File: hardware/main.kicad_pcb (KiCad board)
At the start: 2 copper layers, 80 x 68.3 mm, 17 parts, among them J3 Conn_01x01_Pin, J4 Conn_01x01_Pin, J5 Conn_01x01_Pin, J6 Conn_01x01_Pin, K2 ADW11

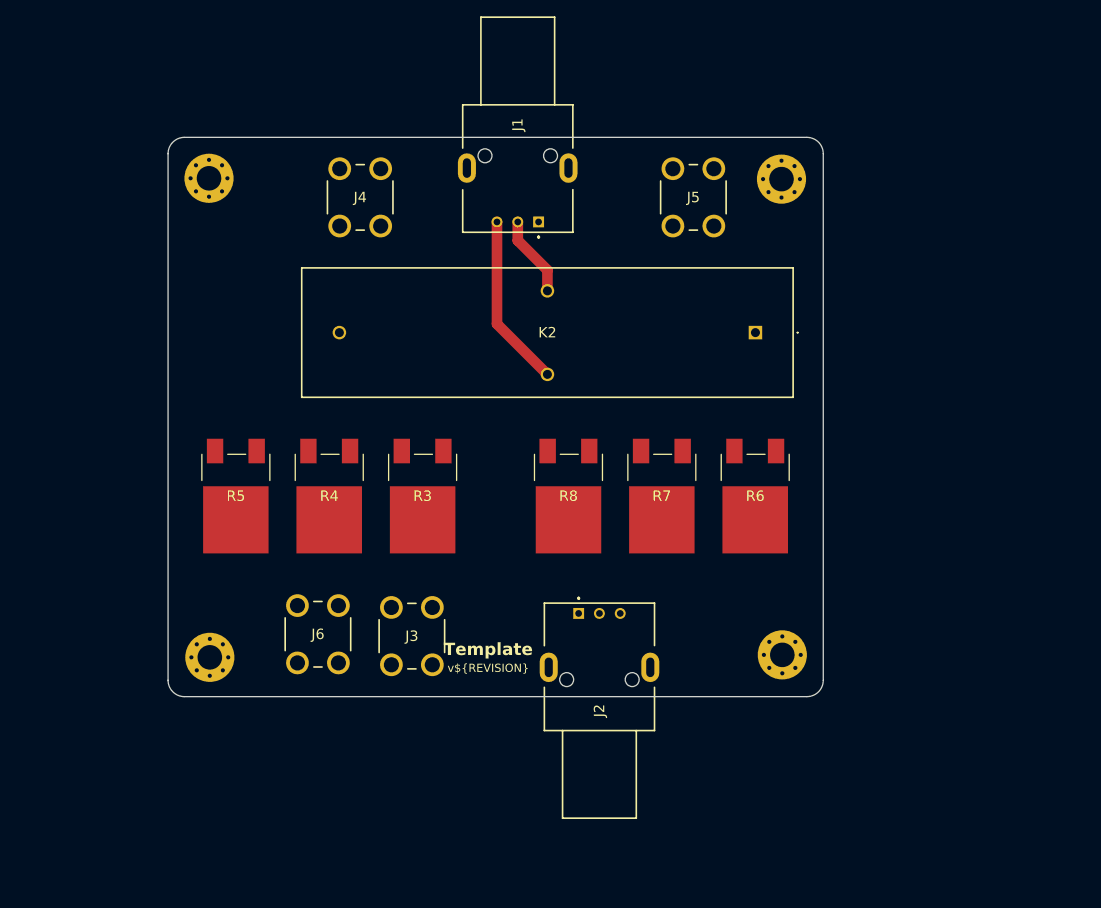
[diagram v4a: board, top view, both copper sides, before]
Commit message: changed resistors
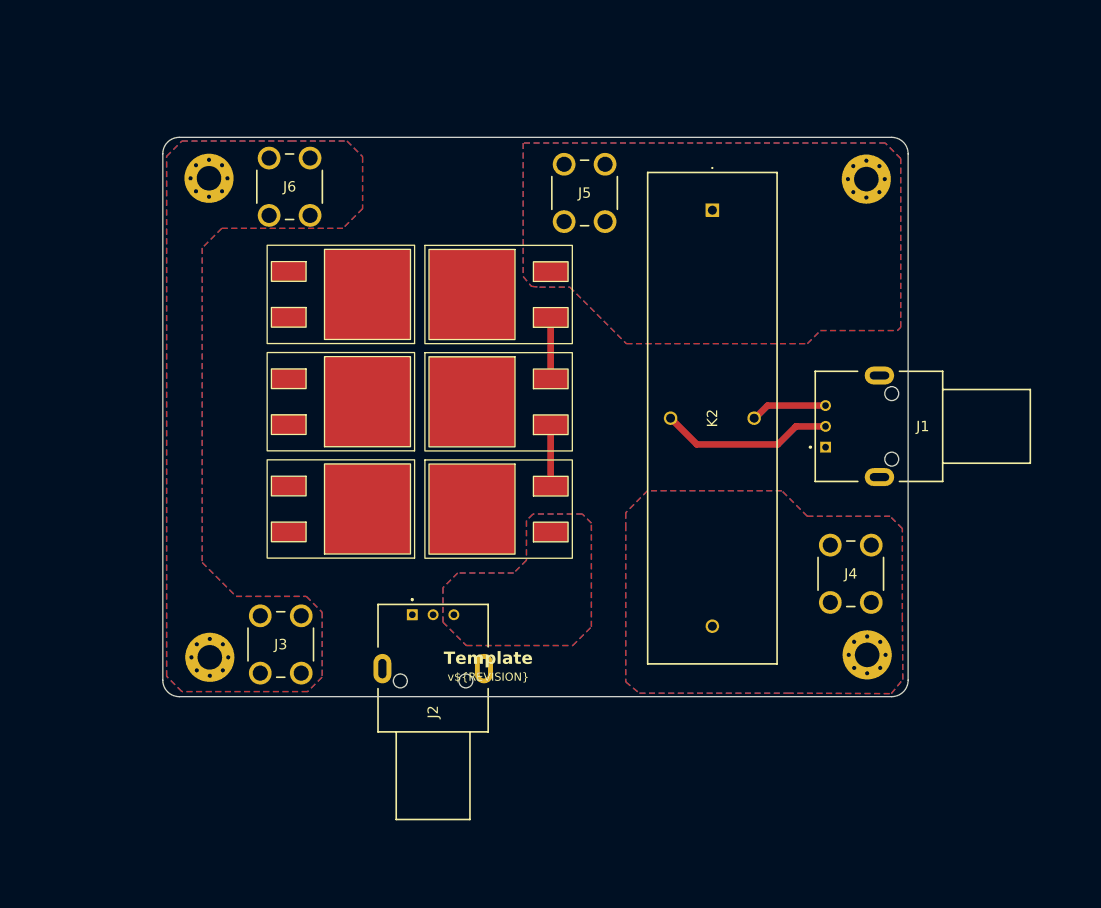
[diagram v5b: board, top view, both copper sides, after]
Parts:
- removed R3, R4, R5, R6, R7, R8: TKH45P5K00FE-TR, TKH45P5K00FE-TR:TKH45P50R0FETR
- added PWR263S-35-5001F1: ~, 7696:PWR263S-35-5001F, F.Cu at (135.7, 66.9)
- added PWR263S-35-5001F2: ~, 7696:PWR263S-35-5001F, F.Cu at (135.7, 80.0)
- added PWR263S-35-5001F3: ~, 7696:PWR263S-35-5001F, F.Cu at (135.7, 93.1)
- added PWR263S-35-5001F4: ~, 7696:PWR263S-35-5001F, F.Cu at (159.0, 93.1)
- added PWR263S-35-5001F5: ~, 7696:PWR263S-35-5001F, F.Cu at (159.0, 80.0)
- added PWR263S-35-5001F6: ~, 7696:PWR263S-35-5001F, F.Cu at (159.0, 66.9)
- moved J4 75.5 mm to (197.5, 104.5)
- moved J6 54.7 mm to (134.0, 50.2)
- moved J1 44.5 mm to (196.9, 85.5), turned to 0 degrees
- moved J2 20.3 mm to (146.5, 106.0)
- moved J3 16.0 mm to (132.9, 106.1)
- moved K2 15.8 mm to (183.1, 56.6), turned to -90 degrees
- moved J5 13.3 mm to (165.0, 58.0)
- moved REF** 10.4 mm to (201.9, 52.8)
- moved REF** 10.4 mm to (202.0, 110.9)
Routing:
- net GND: track 21.2 -> 9.50 mm
- net SD+: track 9.91 -> 21.2 mm
- net Net-(PWR263S-35-5001F5-Pad2): track 0.00 -> 7.50 mm
- net Net-(PWR263S-35-5001F4-Pad2): track 0.00 -> 7.50 mm
- added copper zone on B.Cu, net HV+
- added copper zone on F.Cu, net HV+
- added copper zone on B.Cu, net HV-
- added copper zone on F.Cu, net HV-
- added copper zone on B.Cu, net Net-(J4-Pin_1)
- added copper zone on F.Cu, net Net-(J4-Pin_1)
- added copper zone on B.Cu, net TSMP-
- added copper zone on F.Cu, net TSMP-
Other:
- board size 80 x 68.3 mm -> 91 x 68.3 mm

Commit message: added logo
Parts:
- removed REF** (x4): MountingHole_3mm_Pad_Via, MountingHole:MountingHole_3mm_Pad_Via
- added G***: LOGO, put_silkscreen:SignatureBox25mm, B.Cu at (164.5, 54.7)
- added H1: MountingHole, MountingHole:MountingHole_3.2mm_M3, F.Cu at (208.4, 52.8)
- added H2: MountingHole, MountingHole:MountingHole_3.2mm_M3, F.Cu at (208.5, 110.9)
- added H3: MountingHole, MountingHole:MountingHole_3.2mm_M3, F.Cu at (120.4, 52.7)
- added H4: MountingHole, MountingHole:MountingHole_3.2mm_M3, F.Cu at (120.5, 111.2)
- moved J5 40.2 mm to (204.0, 67.5)
- moved J6 14.0 mm to (124.5, 60.5)
- moved J3 12.8 mm to (124.5, 96.5)
- moved J4 6.62 mm to (204.0, 103.5)
- moved J1 6.54 mm to (203.5, 85.5)
- moved J2 6.54 mm to (153.0, 106.0)
- moved K2 6.54 mm to (189.6, 56.6)
- moved PWR263S-35-5001F1 6.54 mm to (142.3, 66.9)
- moved PWR263S-35-5001F2 6.54 mm to (142.3, 80.0)
- moved PWR263S-35-5001F3 6.54 mm to (142.3, 93.1)
- moved PWR263S-35-5001F4 6.54 mm to (165.5, 93.1)
- moved PWR263S-35-5001F5 6.54 mm to (165.5, 80.0)
- moved PWR263S-35-5001F6 6.54 mm to (165.5, 66.9)
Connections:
- PWR263S-35-5001F1 pad 1: TSMP+ -> HV+
- PWR263S-35-5001F3 pad 2: HV+ -> TSMP+
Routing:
- net HV-: track 0.00 -> 22.9 mm, vias 0 -> 24
- net TSMP+: track 0.00 -> 22.8 mm
- net TSMP-: track 0.00 -> 19.6 mm
- net HV+: track 0.00 -> 14.9 mm, vias 0 -> 30
- net Net-(PWR263S-35-5001F1-Pad2): track 0.01 -> 7.50 mm
- net Net-(PWR263S-35-5001F2-Pad2): track 0.01 -> 7.50 mm
- net Net-(J4-Pin_1): vias 0 -> 25
- added copper zone on B.Cu, net /THERMO
- added copper zone on F.Cu, net /THERMO
- removed copper zone on B.Cu, net TSMP-
- removed copper zone on F.Cu, net TSMP-
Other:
- board size 91 x 68.3 mm -> 98 x 68.3 mm

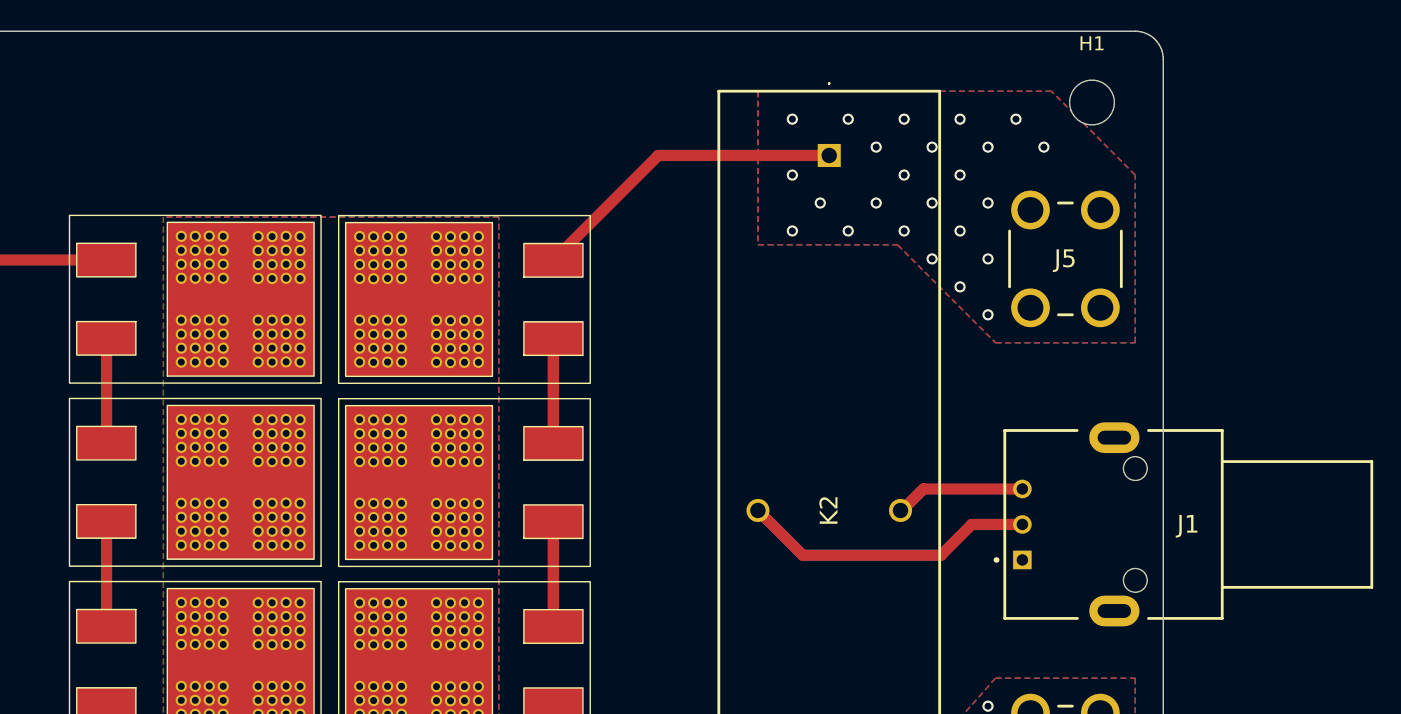
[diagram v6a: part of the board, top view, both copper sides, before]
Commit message: updated schematic with measures
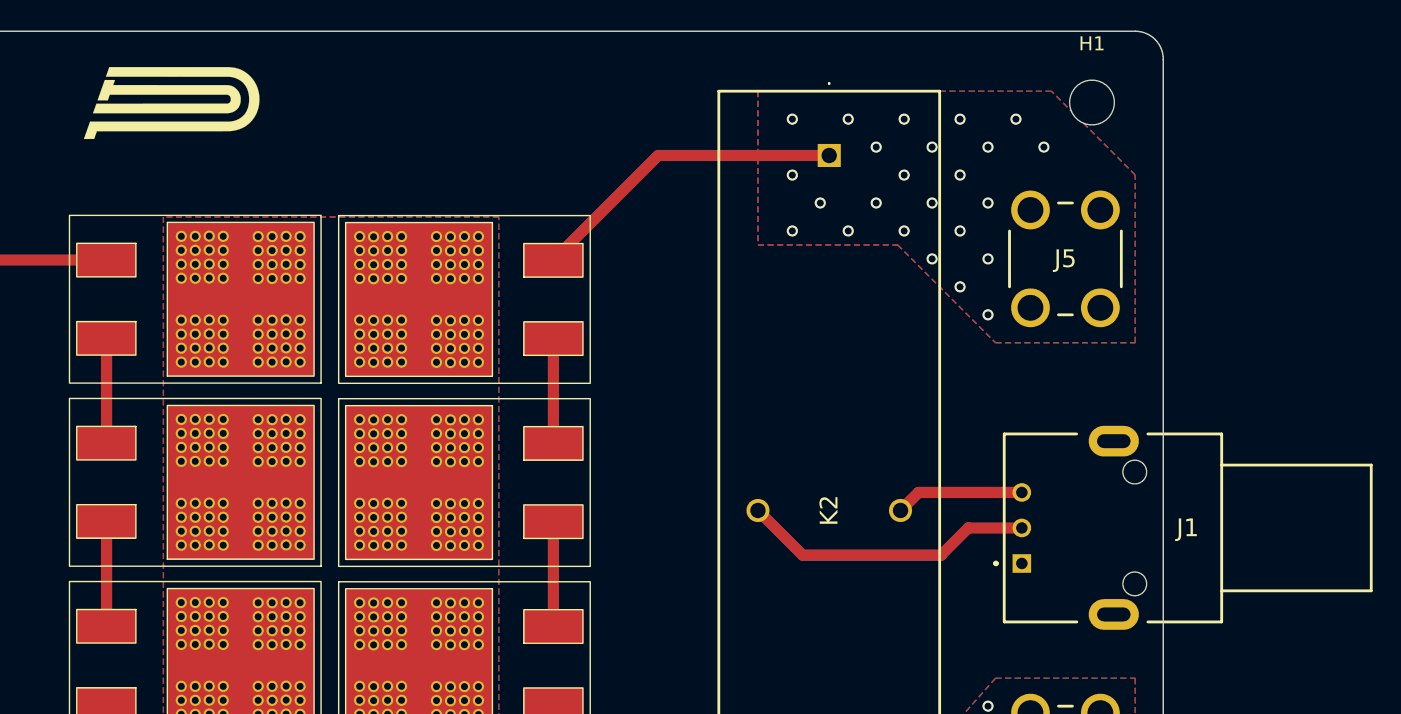
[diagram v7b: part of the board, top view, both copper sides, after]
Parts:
- added G***: LOGO, put_silkscreen:PUTM_LOGO_15mm, F.Cu at (142.2, 52.7)
- moved J1 0.25 mm to (203.4, 85.8)

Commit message: Fabrication Toolkit files added
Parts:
- removed J3: Conn_01x01_Pin, 7696:7696
- moved G*** 59.6 mm to (124.5, 109.6)
- moved J4 17.3 mm to (187.5, 108.5)
- moved K2 16.7 mm to (173.0, 57.6)
- moved J5 15.8 mm to (188.5, 64.5)
- moved G*** 14.6 mm to (150.0, 53.0)
- moved J2 14.6 mm to (138.5, 107.7)
- moved PWR263S-35-5001F2 14.6 mm to (127.7, 81.6)
- moved PWR263S-35-5001F3 14.6 mm to (127.7, 94.7)
- moved PWR263S-35-5001F4 14.6 mm to (151.0, 94.8)
- moved PWR263S-35-5001F5 14.6 mm to (151.0, 81.7)
- moved PWR263S-35-5001F1 14.6 mm to (127.7, 68.5)
- moved PWR263S-35-5001F6 14.6 mm to (151.0, 68.6)
- moved J6 11.6 mm to (127.5, 49.3)
- moved H4 8.79 mm to (112.0, 113.3)
- moved H3 8.71 mm to (111.9, 51.0)
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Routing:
- net GND: track 9.31 -> 20.0 mm
- net SD+: track 21.0 -> 31.6 mm
- net HV+: track 14.9 -> 9.82 mm, vias 30 -> 0
- net HV-: track 22.9 -> 21.0 mm
- net Net-(J4-Pin_1): vias 25 -> 24
- removed copper zone on B.Cu, net HV+
- removed copper zone on F.Cu, net HV+
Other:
- board size 98 x 68.3 mm -> 100 x 72.4 mm
- board text added: "HV+"
- board text added: "HV-"
- board text added: "LV"
- board text added: "TS"
- board text removed: "Template"
- board text removed: "v${REVISION}"
